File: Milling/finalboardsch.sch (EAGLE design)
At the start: 23 parts, among them IC1 317EMP, X1 332-02, X10 332-02, X11 332-02, X2 332-02, X3 332-02, X4 332-02, X5 332-02, X6 332-02, X7 332-02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

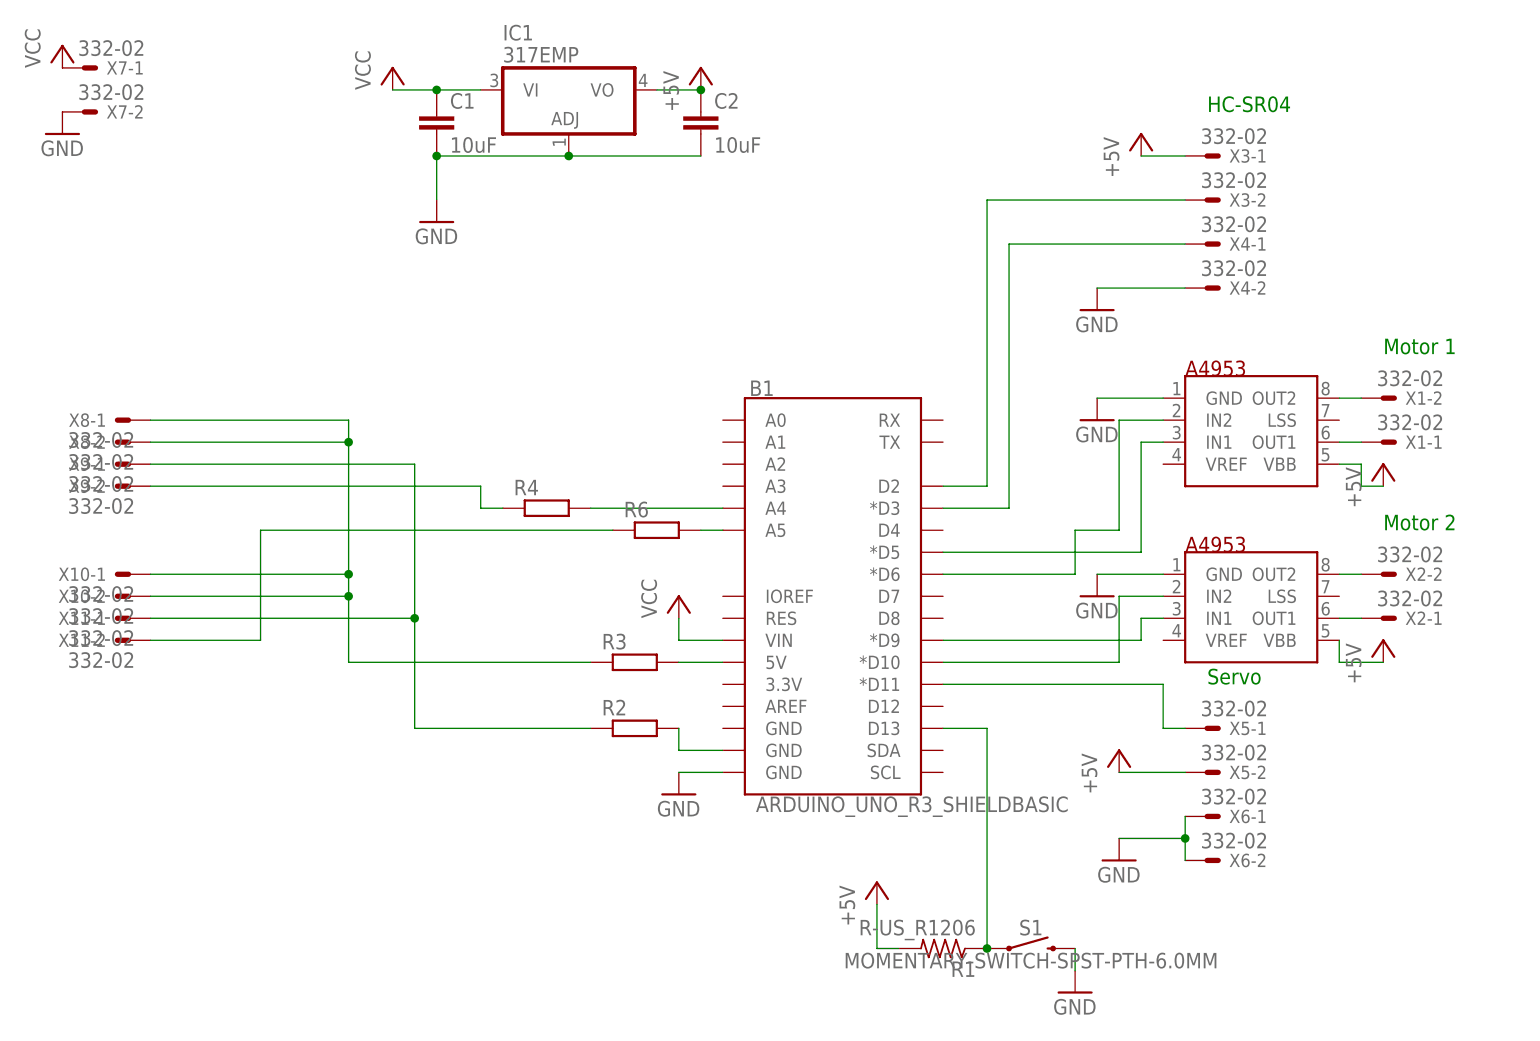
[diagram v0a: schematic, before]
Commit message: fixed eagle files
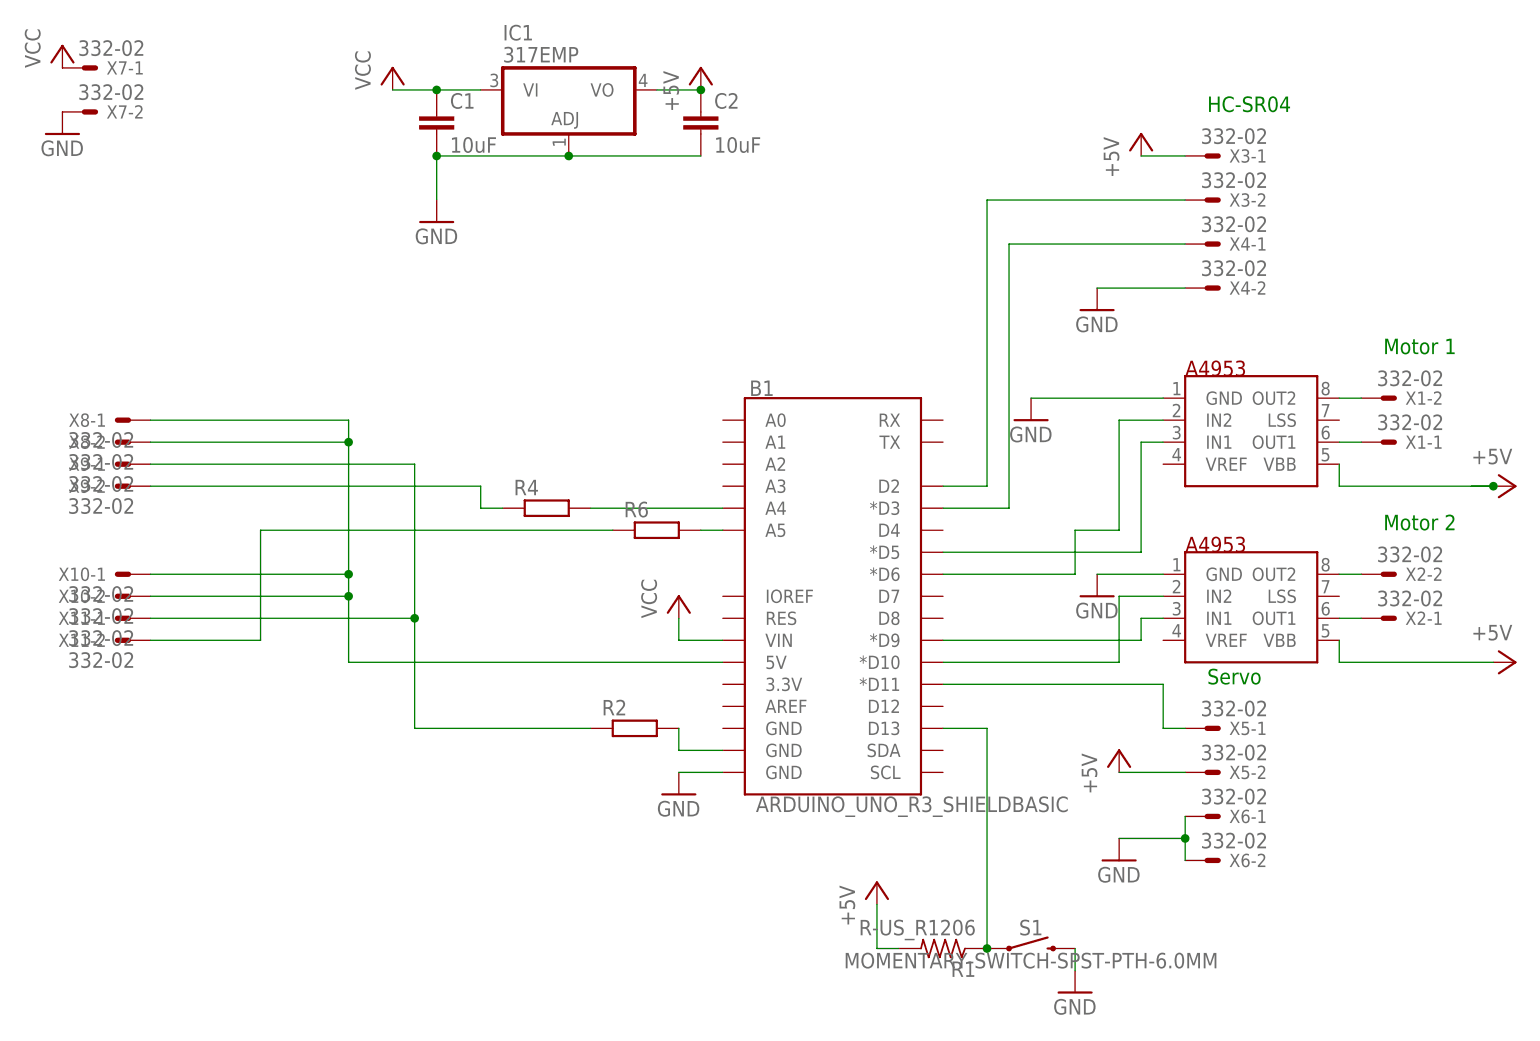
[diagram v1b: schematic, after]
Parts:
- removed R3: (no value), eagle-ltspice:RR1206
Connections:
- removed net N$14: R3.1, X10-1.S, X10-2.S, X8-1.S, X8-2.S
- net N$18: now also X10-1.S, X10-2.S, X8-1.S, X8-2.S; no longer R3.2
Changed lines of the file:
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@@
 <?xml version="1.0" encoding="utf-8"?>
 <!DOCTYPE eagle SYSTEM "eagle.dtd">
-<eagle version="8.7.1">
+<eagle version="8.7.0">
 <drawing>
 <settings>
@@
 <part name="X11" library="con-garry" library_urn="urn:adsk.eagle:library:147" deviceset="332-02" device="" package3d_urn="urn:adsk.eagle:package:6810/1"/>
 <part name="R2" library="eagle-ltspice" library_urn="urn:adsk.eagle:library:217" deviceset="R" device="R1206" package3d_urn="urn:adsk.eagle:package:13301/1"/>
-<part name="R3" library="eagle-ltspice" library_urn="urn:adsk.eagle:library:217" deviceset="R" device="R1206" package3d_urn="urn:adsk.eagle:package:13301/1"/>
 <part name="R4" library="eagle-ltspice" library_urn="urn:adsk.eagle:library:217" deviceset="R" device="R1206" package3d_urn="urn:adsk.eagle:package:13301/1"/>
 <part name="R6" library="eagle-ltspice" library_urn="urn:adsk.eagle:library:217" deviceset="R" device="R1206" package3d_urn="urn:adsk.eagle:package:13301/1"/>
@@
 <instance part="A1" gate="G$1" x="40.64" y="55.88"/>
 <instance part="A2" gate="G$1" x="40.64" y="35.56"/>
-<instance part="GND2" gate="1" x="30.48" y="50.8"/>
+<instance part="GND2" gate="1" x="22.86" y="50.8"/>
 <instance part="GND3" gate="1" x="30.48" y="30.48"/>
 <instance part="X1" gate="-1" x="63.5" y="48.26"/>
@@
 <instance part="GND5" gate="1" x="30.48" y="63.5"/>
 <instance part="P+4" gate="1" x="35.56" y="83.82"/>
-<instance part="P+5" gate="1" x="63.5" y="45.72"/>
-<instance part="P+6" gate="1" x="63.5" y="25.4"/>
+<instance part="P+5" gate="1" x="78.74" y="43.18" rot="R270"/>
+<instance part="P+6" gate="1" x="78.74" y="22.86" rot="R270"/>
 <instance part="X5" gate="-1" x="43.18" y="15.24"/>
 <instance part="X5" gate="-2" x="43.18" y="10.16"/>
@@
 <instance part="X11" gate="-2" x="-81.28" y="25.4" rot="R180"/>
 <instance part="R2" gate="G$1" x="-22.86" y="15.24"/>
-<instance part="R3" gate="G$1" x="-22.86" y="22.86"/>
 <instance part="R4" gate="G$1" x="-33.02" y="40.64"/>
 <instance part="R6" gate="G$1" x="-20.32" y="38.1"/>
@@
 <pinref part="A1" gate="G$1" pin="GND"/>
 <pinref part="GND2" gate="1" pin="GND"/>
-<wire x1="38.1" y1="53.34" x2="30.48" y2="53.34" width="0.1524" layer="91"/>
+<wire x1="38.1" y1="53.34" x2="22.86" y2="53.34" width="0.1524" layer="91"/>
 </segment>
 <segment>
@@
 </segment>
 <segment>
-<pinref part="A1" gate="G$1" pin="VBB"/>
-<wire x1="58.42" y1="45.72" x2="60.96" y2="45.72" width="0.1524" layer="91"/>
-<wire x1="60.96" y1="45.72" x2="60.96" y2="43.18" width="0.1524" layer="91"/>
-<pinref part="P+5" gate="1" pin="+5V"/>
-<wire x1="60.96" y1="43.18" x2="63.5" y2="43.18" width="0.1524" layer="91"/>
-</segment>
-<segment>
-<pinref part="A2" gate="G$1" pin="VBB"/>
-<wire x1="58.42" y1="25.4" x2="58.42" y2="22.86" width="0.1524" layer="91"/>
-<wire x1="58.42" y1="22.86" x2="63.5" y2="22.86" width="0.1524" layer="91"/>
-<pinref part="P+6" gate="1" pin="+5V"/>
-</segment>
-<segment>
 <pinref part="P+7" gate="1" pin="+5V"/>
 <pinref part="X5" gate="-2" pin="S"/>
@@
 <pinref part="R1" gate="G$1" pin="2"/>
 <wire x1="7.62" y1="-10.16" x2="5.08" y2="-10.16" width="0.1524" layer="91"/>
+</segment>
+<segment>
+<pinref part="P+6" gate="1" pin="+5V"/>
+<pinref part="A2" gate="G$1" pin="VBB"/>
+<wire x1="58.42" y1="25.4" x2="58.42" y2="22.86" width="0.1524" layer="91"/>
+<wire x1="76.2" y1="22.86" x2="58.42" y2="22.86" width="0.1524" layer="91"/>
+</segment>
+<segment>
+<pinref part="P+5" gate="1" pin="+5V"/>
+<wire x1="73.66" y1="43.18" x2="76.2" y2="43.18" width="0.1524" layer="91"/>
+<pinref part="A1" gate="G$1" pin="VBB"/>
+<wire x1="58.42" y1="45.72" x2="58.42" y2="43.18" width="0.1524" layer="91"/>
+<wire x1="58.42" y1="43.18" x2="76.2" y2="43.18" width="0.1524" layer="91"/>
+<junction x="76.2" y="43.18"/>
 </segment>
 </net>
@@
 </segment>
 </net>
-<net name="N$10" class="0">
-<segment>
-<pinref part="X3" gate="-2" pin="S"/>
-<wire x1="40.64" y1="76.2" x2="17.78" y2="76.2" width="0.1524" layer="91"/>
-<wire x1="17.78" y1="76.2" x2="17.78" y2="43.18" width="0.1524" layer="91"/>
-<pinref part="B1" gate="G$1" pin="D2"/>
-<wire x1="17.78" y1="43.18" x2="12.7" y2="43.18" width="0.1524" layer="91"/>
-</segment>
-</net>
 <net name="N$11" class="0">
 <segment>
@@
 <segment>
 <pinref part="B1" gate="G$1" pin="5V"/>
-<pinref part="R3" gate="G$1" pin="2"/>
-<wire x1="-12.7" y1="22.86" x2="-17.78" y2="22.86" width="0.1524" layer="91"/>
-</segment>
-</net>
-<net name="N$13" class="0">
-<segment>
-<pinref part="R4" gate="G$1" pin="2"/>
-<pinref part="B1" gate="G$1" pin="A4"/>
-<wire x1="-27.94" y1="40.64" x2="-12.7" y2="40.64" width="0.1524" layer="91"/>
-</segment>
-</net>
-<net name="N$19" class="0">
-<segment>
-<pinref part="B1" gate="G$1" pin="A5"/>
-<pinref part="R6" gate="G$1" pin="2"/>
-<wire x1="-15.24" y1="38.1" x2="-12.7" y2="38.1" width="0.1524" layer="91"/>
-</segment>
-</net>
-<net name="N$14" class="0">
-<segment>
-<pinref part="R3" gate="G$1" pin="1"/>
-<wire x1="-27.94" y1="22.86" x2="-55.88" y2="22.86" width="0.1524" layer="91"/>
+<wire x1="-12.7" y1="22.86" x2="-55.88" y2="22.86" width="0.1524" layer="91"/>
 <wire x1="-55.88" y1="22.86" x2="-55.88" y2="30.48" width="0.1524" layer="91"/>
 <pinref part="X10" gate="-1" pin="S"/>
@@
 </segment>
 </net>
+<net name="N$13" class="0">
+<segment>
+<pinref part="R4" gate="G$1" pin="2"/>
+<pinref part="B1" gate="G$1" pin="A4"/>
+<wire x1="-27.94" y1="40.64" x2="-12.7" y2="40.64" width="0.1524" layer="91"/>
+</segment>
+</net>
+<net name="N$19" class="0">
+<segment>
+<pinref part="B1" gate="G$1" pin="A5"/>
+<pinref part="R6" gate="G$1" pin="2"/>
+<wire x1="-15.24" y1="38.1" x2="-12.7" y2="38.1" width="0.1524" layer="91"/>
+</segment>
+</net>
 <net name="N$15" class="0">
 <segment>
@@
 </segment>
 </net>
+<net name="N$21" class="0">
+<segment>
+<pinref part="X3" gate="-2" pin="S"/>
+<pinref part="B1" gate="G$1" pin="D2"/>
+<wire x1="17.78" y1="43.18" x2="12.7" y2="43.18" width="0.1524" layer="91"/>
+<wire x1="17.78" y1="76.2" x2="17.78" y2="43.18" width="0.1524" layer="91"/>
+<wire x1="40.64" y1="76.2" x2="17.78" y2="76.2" width="0.1524" layer="91"/>
+</segment>
+</net>
